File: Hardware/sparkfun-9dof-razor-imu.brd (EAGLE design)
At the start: 40.6 x 27.9 mm, 40 parts, among them J1 AVR_SPI_PRG_6PTH, Q1 8MHz, U1 ITG-32001:1, U2 ADXL3451:1, U5 3.3V, U6 ATMEGA328

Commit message: Initial commit of v24.
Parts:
- removed C13, C22, C24, C25, C27, C29: 0.1uF, SparkFun:0603-CAP
- removed C18: 0.22uF, SparkFun:0603-CAP
- removed C21: 4.7uF, SparkFun:0603-CAP
- removed C23, C26: 10uF, SparkFun:EIA3216
- removed JP10: JST_Horizontal, SparkFun:1X02
- removed JP11, JP12: FIDUCIAL1X2.5, abes:FIDUCIAL-1X2.5
- removed JP2, JP4, JP6: STAND-OFF, SparkFun:STAND-OFF
- removed JP3: LOGO-SFENEW, SparkFun:SFE-NEW-WEBLOGO
- removed JP7: FTDI Basic, SparkFun:1X06
- removed LED1: Red, SparkFun:LED-0603
- removed Q1: 8MHz, SparkFun:RESONATOR-SMD
- removed R11: 10K, SparkFun:0603-RES
- removed R12: 330, SparkFun:0603-RES
- removed S2: Power, SparkFun:AYZ0202
- removed U$1: HMC5883LSMD, SparkFun:16LPCC
- removed U$4: OSHW-LOGOL, SparkFun:OSHW-LOGO-L
- removed U5: 3.3V, SparkFun:SOT23-5
- removed U6: ATMEGA328, SparkFun:TQFP32-08
- added C10: 2.2uF, SparkFun-Capacitors:0603
- added C11, C12: 4.7uF, SparkFun-Capacitors:0603
- added C4, C5, C6: 0.1uF, SparkFun-Capacitors:0603
- added C7, C8: 15pF, SparkFun-Capacitors:0603
- added C9: 1.0uF, SparkFun-Capacitors:0603
- added D1: 1A/23V/620mV, SparkFun-DiscreteSemi:SOD-323
- added D2: RED, SparkFun-LED:LED-0603
- added D4: Yellow, SparkFun-LED:LED-0603
- added F1: 6V/0.5A, SparkFun-Fuses:1206
- added FRAME1: FRAME-LEDGER, SparkFun-Aesthetics:CREATIVE_COMMONS
- added H1, H2, H3, H4: STAND-OFF, SparkFun-Electromechanical:STAND-OFF
- added J2: (no value), SparkFun-Connectors:JST-2-SMD
- added J3: (no value), SparkFun-Connectors:1X04
- added J4: (no value), SparkFun-Connectors:USB-B-MICRO-SMD_V03
- added J5, J7: (no value), SparkFun-Connectors:1X06_NO_SILK
- added J8: (no value), SparkFun-Connectors:1X08
- added LOGO1: SFE_LOGO_FLAME.1_INCH, SparkFun-Aesthetics:SFE_LOGO_FLAME_.1
- added LOGO2: OSHW-LOGOS, SparkFun-Aesthetics:OSHW-LOGO-S
- added LOGO3: SFE_LOGO_NAME.1_INCH, SparkFun-Aesthetics:SFE_LOGO_NAME_.1
- added R3, R5: 1k, SparkFun-Resistors:0603
- added R4: 10k, SparkFun-Resistors:0603
- added R7, R8: 100k, SparkFun-Resistors:0603
- added R9: 2.2k, SparkFun-Resistors:0603
- added U3: 3.3V, SparkFun-IC-Power:SOT23-5
- added U4: MCP73831, SparkFun-IC-Power:SOT23-5
- added Y1: 32.768kHz, SparkFun-Clocks:CRYSTAL-SMD-3.2X1.5MM
- C1: device SparkFun:0603-CAP -> SparkFun-Capacitors:0603
- C2: value 2.2nF -> 0.1uF; device SparkFun:0603-CAP -> SparkFun-Capacitors:0603
- C3: value 10nF -> 0.1uF; device SparkFun:0603-CAP -> SparkFun-Capacitors:0603
- D3: value Green -> BLUE; device SparkFun:LED-0603 -> SparkFun-LED:LED-0603
- J1: value AVR_SPI_PRG_6PTH -> USD_CONNECTOR; device SparkFun:2X3 -> SparkFun-Connectors:MICRO-SD-SOCKET-PP
- JP1: value JST_Horizontal -> PWR-SELECT; device SparkFun:JST-2-SMD -> SparkFun-Jumpers:SMT-JUMPER_3_1-NC_PASTE_NO-SILK
- JP5: value STAND-OFF -> CORTEX_DEBUGPTH; device SparkFun:STAND-OFF -> samd21-temp:2X5-PTH-1.27MM
- R1: device SparkFun:0603-RES -> SparkFun-Resistors:0603
- R10: value 10K -> 1k; device SparkFun:0603-RES -> SparkFun-Resistors:0603
- R2: value 4.7K -> 4.7k; device SparkFun:0603-RES -> SparkFun-Resistors:0603
- S1: value Reset -> (none); device SparkFun:TACTILE_SWITCH_SMD -> SparkFun-Electromechanical:SWITCH-SPST-SMD-A
- U1: value ITG-32001:1 -> ATSAMD21G-A; device Testing:QFN-24_ITG3200_1:1 -> SparkFun-IC-Microcontroller:TQFP-48
- U2: value ADXL3451:1 -> MPU-9250"; device Testing:LGA14 -> 9dof-devboard-temp:QFN24-3X3
- moved JP5 30.7 mm to (7.62, 21.6), turned to 270 degrees
- moved D3 28.5 mm to (28.6, 7.62), flipped to the bottom, turned to 90 degrees
- moved C2 27.6 mm to (16.5, 28.6), turned to 180 degrees
- moved S1 24.0 mm to (2.79, 10.9), flipped to the bottom, turned to 270 degrees
- moved JP1 22.9 mm to (24.1, 29.2)
- moved C1 21.7 mm to (20.3, 25.4)
- moved R1 19.8 mm to (11.2, 26.7), turned to 90 degrees
- moved R2 18.9 mm to (12.7, 26.7), turned to 90 degrees
- moved R10 16.7 mm to (16.5, 3.68), flipped to the bottom, turned to 90 degrees
- moved U2 14.2 mm to (16.5, 25.4), turned to 90 degrees
- moved U1 10.3 mm to (15.2, 12.1), turned to 180 degrees
- moved J1 9.91 mm to (9.91, 14.2), flipped to the bottom
- moved C3 3.42 mm to (17.8, 4.45), turned to 270 degrees
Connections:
- removed net DTR: C27.2, JP7.1
- removed net MISO: J1.1, U6.16
- removed net MOSI: J1.4, U6.15
- removed net N$12: D3.A, R12.2
- removed net N$13: Q1.1, U6.8
- removed net N$14: Q1.3, U6.7
- removed net N$15: JP1.2, JP10.2, S2.2, S2.5
- removed net N$38: LED1.A, R11.1
- removed net RAW: C26.A, S2.1, S2.4, U5.1, U5.3
- removed net RESET: C27.1, J1.5, R10.1, S1.3, U6.29
- removed net RXI: JP7.3, U6.30
- removed net SCK: J1.3, R12.1, U6.17
- removed net TXO: JP7.2, U6.31
- new net !RESET: JP5.10, R4.1, U1.40
- new net A0: J8.1, U1.3
- new net A1: J8.2, U1.7
- new net A2: U1.8
- new net A3: U1.9
- new net A4: U1.10
- new net A5: U1.47
- new net CHG_LED: R10.1, U4.1
- new net D0/RXI: J8.8, U1.16
- new net D1/TXO: J8.7, U1.15
- new net D10: J8.6, U1.27
- new net D11: J8.5, U1.25
- new net D12: J8.4, U1.28
- new net D13: J8.3, R3.2, U1.26
- new net D2/SD_CD: J1.CD1, U1.23
- new net D3: U1.14
- new net D4: U1.13
- new net D5: U1.24
- new net D6: U1.29
- new net D7: U1.30
- new net D8: U1.11
- new net D9: U1.12
- new net FSYNC: U2.11
- new net INT: U2.12
- new net N$10: C11.1, D1.A, J2.2, U4.3
- new net N$11: D4.C, R10.2
- new net N$5: D2.A, R5.1
- new net N$7: R9.2, U4.5
- new net N$8: J1.RSV1, R7.1
- new net N$9: J1.RSV2, R8.1
- new net REGOUT: C1.1, U2.10
- new net RX_EDBG: U1.38
- new net RX_LED: U1.48
- new net SD_!CS!: J1.CS, U1.22
- new net SD_MISO: J1.DO, U1.21
- new net SD_MOSI: J1.DI, U1.19
- new net SD_SCK: J1.SCLK, U1.20
- new net SHIELD: J4.SHIELD1, J4.SHIELD2, J4.SHIELD3
- new net SWCLK: JP5.4, U1.45
- new net SWDIO: JP5.2, U1.46
- new net TX_EDBG: U1.37
- new net TX_LED: U1.39
- new net USB_D+: J4.D+, U1.34
- new net USB_D-: J4.D-, U1.33
- new net USB_HOST_EN: U1.41
- new net VDDCORE: C4.1, U1.43
- new net VIN: C12.1, C9.1, D1.C, D4.A, F1.2, JP1.1, S1.1, U3.1, U4.4
- new net VREG_EN: S1.2, U3.3
- net 3.3V: now also C10.1, C2.1, C5.1, C6.1, J1.VCC, J3.2, JP1.3, JP5.1, R4.2, R5.2, R7.2, R8.2, U1.17, U1.36, U1.44, U1.6, U2.13, U2.22, U2.8, U3.5; no longer C13.1, C22.1, C23.A, C24.2, C29.1, J1.2, JP7.4, R10.2, R11.2, U$1.13, U$1.2, U$1.4, U1.13, U1.8, U2.1, U2.6, U2.7, U5.5, U6.18, U6.4, U6.6
- net AREF: now also U1.4; no longer C25.2, U6.20
- net GND: now also C10.2, C11.2, C12.2, C4.2, C5.2, C6.2, C7.1, C8.2, C9.2, D2.C, J1.GND, J1.GND1, J1.GND3, J2.1, J3.1, J4.GND, J7.1, J7.2, J7.3, J7.4, J7.5, J7.6, JP5.3, JP5.5, R9.1, S1.3, U1.35, U1.42, U1.5, U2.18, U2.9, U3.2, U4.2; no longer C13.2, C21.2, C22.2, C23.C, C24.1, C25.1, C26.C, C29.2, J1.6, JP1.1, JP10.1, JP7.5, JP7.6, LED1.C, Q1.2, S1.1, U$1.11, U$1.9, U1.1, U1.11, U1.9, U2.12, U2.2, U2.4, U2.5, U5.2, U6.21, U6.3, U6.5
- net N$1: now also F1.1, J4.VBUS; no longer C18.2, U$1.8
- net N$2: now also C7.2, U1.1, Y1.P$2; no longer C18.1, U$1.12
- net N$3: now also D3.A, R3.1; no longer C1.1, U1.10
- net N$4: now also C8.1, U1.2, Y1.P$1; no longer C2.1, U1.20
- net N$6: now also J5.1, J5.2, J5.3, J5.4, J5.5, J5.6, JP1.2; no longer C21.1, U$1.10
- net SCL: now also J3.4, U1.32, U2.23; no longer U$1.1, U1.23, U2.14, U6.28
- net SDA: now also J3.3, U1.31, U2.24; no longer U$1.16, U1.24, U2.13, U6.27
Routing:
- net VIN: track 0.00 -> 61.8 mm, vias 0 -> 1
- net RESET: track 44.5 -> 0.00 mm, vias 3 -> 0
- net D13: track 0.00 -> 29.7 mm, vias 0 -> 1
- net D10: track 0.00 -> 25.1 mm, vias 0 -> 1
- net D12: track 0.00 -> 23.4 mm, vias 0 -> 1
- net !RESET: track 0.00 -> 23.3 mm
- net D11: track 0.00 -> 23.1 mm, vias 0 -> 1
- net SWDIO: track 0.00 -> 21.5 mm, vias 0 -> 1
- net D0/RXI: track 0.00 -> 20.6 mm, vias 0 -> 1
- net N$15: track 20.4 -> 0.00 mm
- net SWCLK: track 0.00 -> 20.0 mm, vias 0 -> 1
- net CHG_LED: track 0.00 -> 19.9 mm, vias 0 -> 2
- net D1/TXO: track 0.00 -> 18.0 mm, vias 0 -> 1
- net TXO: track 17.8 -> 0.00 mm, vias 1 -> 0
- net SCK: track 17.1 -> 0.00 mm, vias 2 -> 0
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- added copper zone on layer 1, net SHIELD
- added copper zone on layer 16, net SHIELD
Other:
- board size 40.6 x 27.9 mm -> 31.8 x 31.8 mm
- board text added: "0 !RX"
- board text added: "1 !TX"
- board text added: "10"
- board text added: "11"
- board text added: "12"
- board text added: "13"
- board text added: "9DoF Razor IMU"
- board text added: "A0"
- board text added: "A1"
- board text added: "ACCEL GYRO"
- board text added: "CHG"
- board text added: "MAG"
- board text added: "PWR"
- board text added: "SCL"
- board text added: "SDA"
- board text added: "VBUS"
- board text added: "VIN"
- board text added: "v24"
- board text removed: "+"
- board text removed: "-"
- board text removed: "9DOF RAZOR"
- board text removed: "BLK"
- board text removed: "CTS"
- board text removed: "DTR"
- board text removed: "GRN"
- board text removed: "RXI"
- board text removed: "Reset"
- board text removed: "Stat"
- board text removed: "TXO"
- board text removed: "v23"

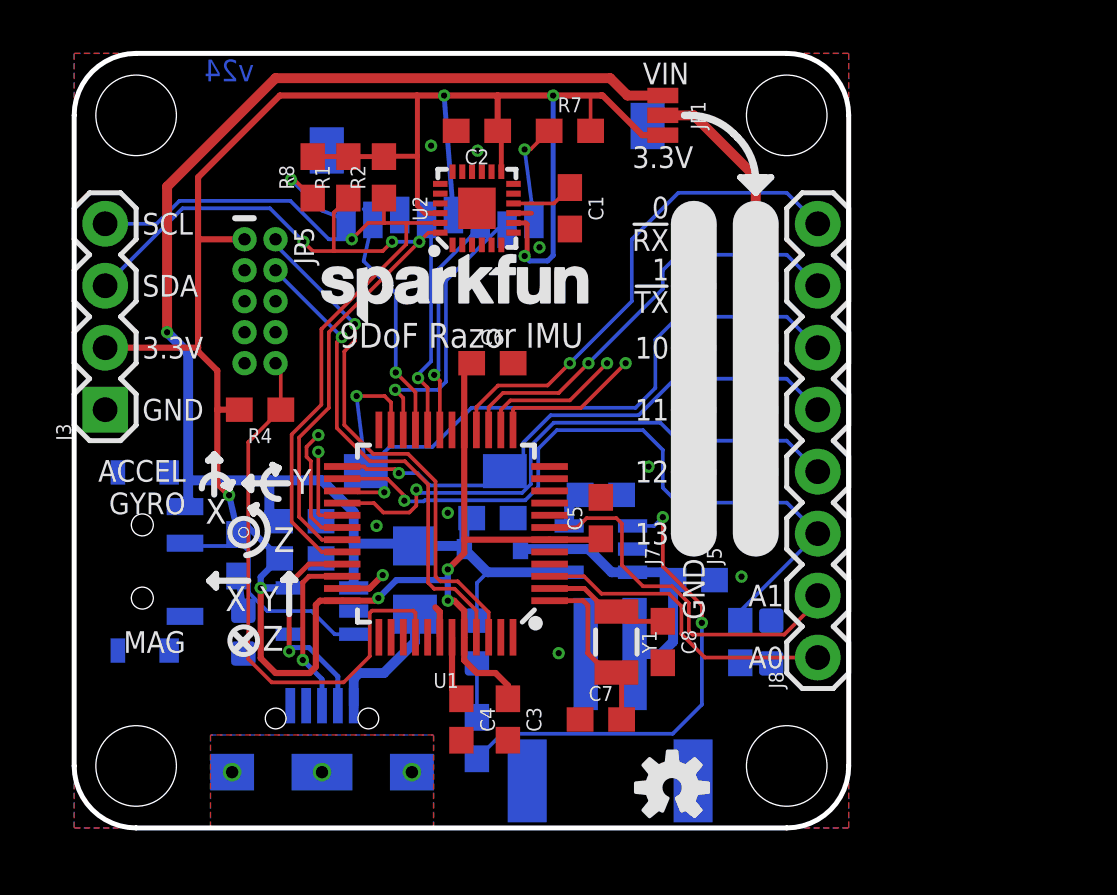
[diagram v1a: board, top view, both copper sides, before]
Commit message: Schematic cleanup, bottom re-routing.
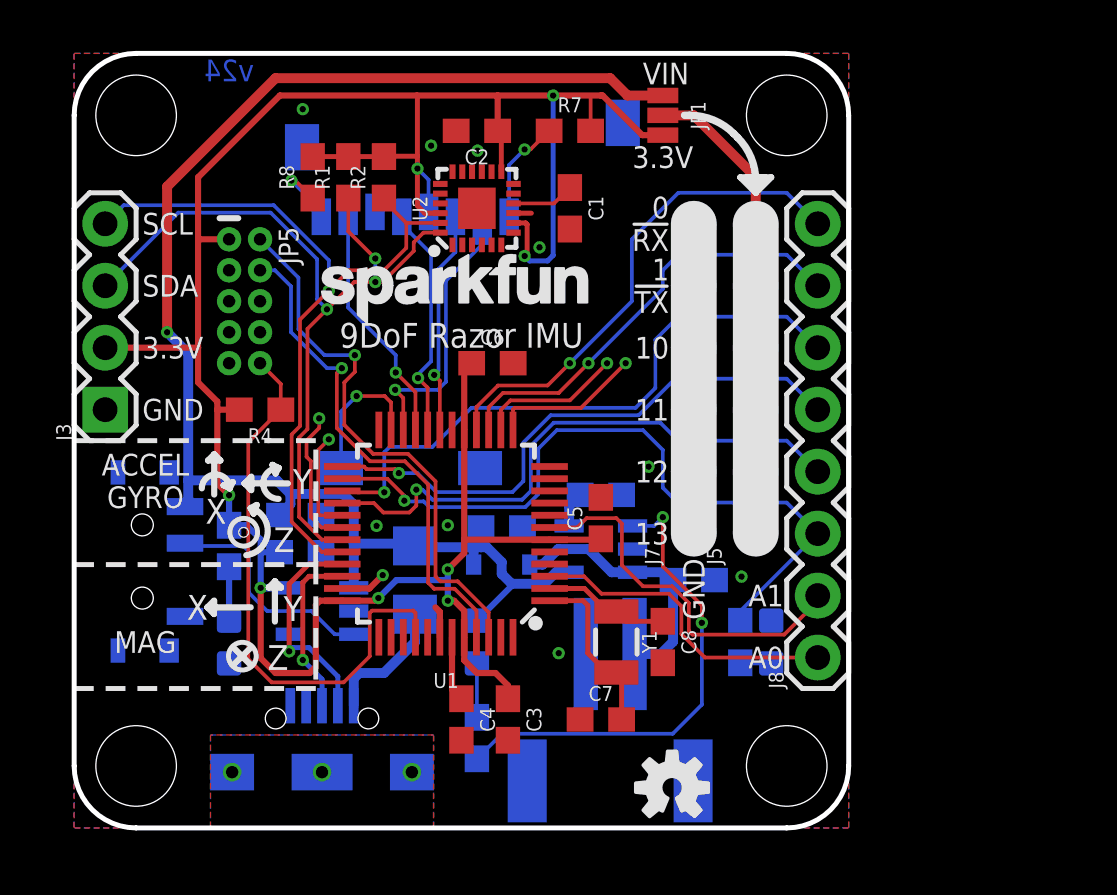
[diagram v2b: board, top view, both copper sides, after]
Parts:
- FRAME1: value FRAME-LEDGER -> FRAME-LETTER
- JP1: value PWR-SELECT -> PW-RAIL
- moved FRAME1 10.2 mm to (20.3, -11.4)
- moved J1 1.02 mm to (8.89, 14.4)
- moved D1 0.74 mm to (17.5, 10.8)
- moved D2 0.71 mm to (6.35, 7.62)
- moved JP5 0.63 mm to (6.99, 21.6)
- moved R5 0.54 mm to (6.35, 11.6)
- moved C12 0.54 mm to (17.5, 12.3)
- moved C10 0.25 mm to (9.27, 11.3)
- moved C9 0.25 mm to (9.27, 12.8)
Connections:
- net USB_D+ renamed D+
- net USB_D- renamed D-
- removed net AREF: U1.4
- removed net RX_EDBG: U1.38
- removed net TX_EDBG: U1.37
- removed net TX_LED: U1.39
- removed net USB_HOST_EN: U1.41
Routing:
- net 3.3V: track 113.3 -> 109.6 mm
- net SWDIO: track 21.5 -> 22.5 mm
- net SWCLK: track 20.0 -> 20.9 mm
- net N$9: track 4.05 -> 3.17 mm
- net SCL: track 32.9 -> 32.1 mm
- net N$5: track 1.44 -> 2.21 mm
- net D7: track 5.09 -> 5.80 mm
- net D6: track 3.55 -> 4.24 mm
- net SD_!CS!: track 11.5 -> 11.0 mm
- net GND: vias 9 -> 10

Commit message: Cleaning up routing.
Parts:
- moved D3 1.27 mm to (27.3, 7.62)
- moved R3 1.27 mm to (28.6, 7.62)
- moved D4 0.64 mm to (15.9, 7.62)
- moved R10 0.64 mm to (15.9, 3.68)
- moved Y1 0.25 mm to (22.0, 7.62)
- moved U4 0.25 mm to (21.6, 11.2)
- moved R9 0.13 mm to (21.6, 13.5), turned to 180 degrees
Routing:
- net D13: track 30.1 -> 26.6 mm
- net D12: track 23.8 -> 22.3 mm
- net N$7: track 1.46 -> 2.73 mm
- net D11: track 23.3 -> 22.4 mm
- net CHG_LED: track 19.9 -> 20.6 mm
- net VIN: track 61.9 -> 62.6 mm
- net GND: track 3.92 -> 3.90 mm, vias 10 -> 11

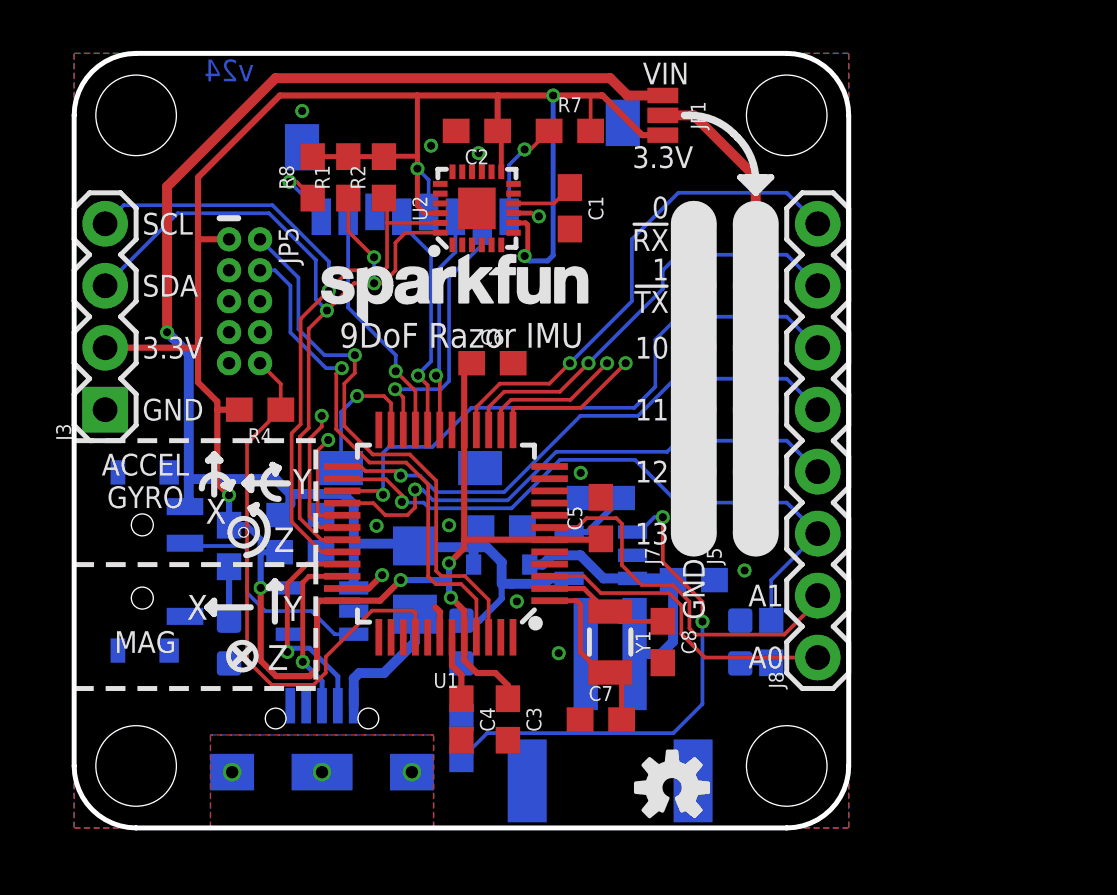
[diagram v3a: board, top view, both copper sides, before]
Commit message: Brd/sch tweaks after engineer checklist.
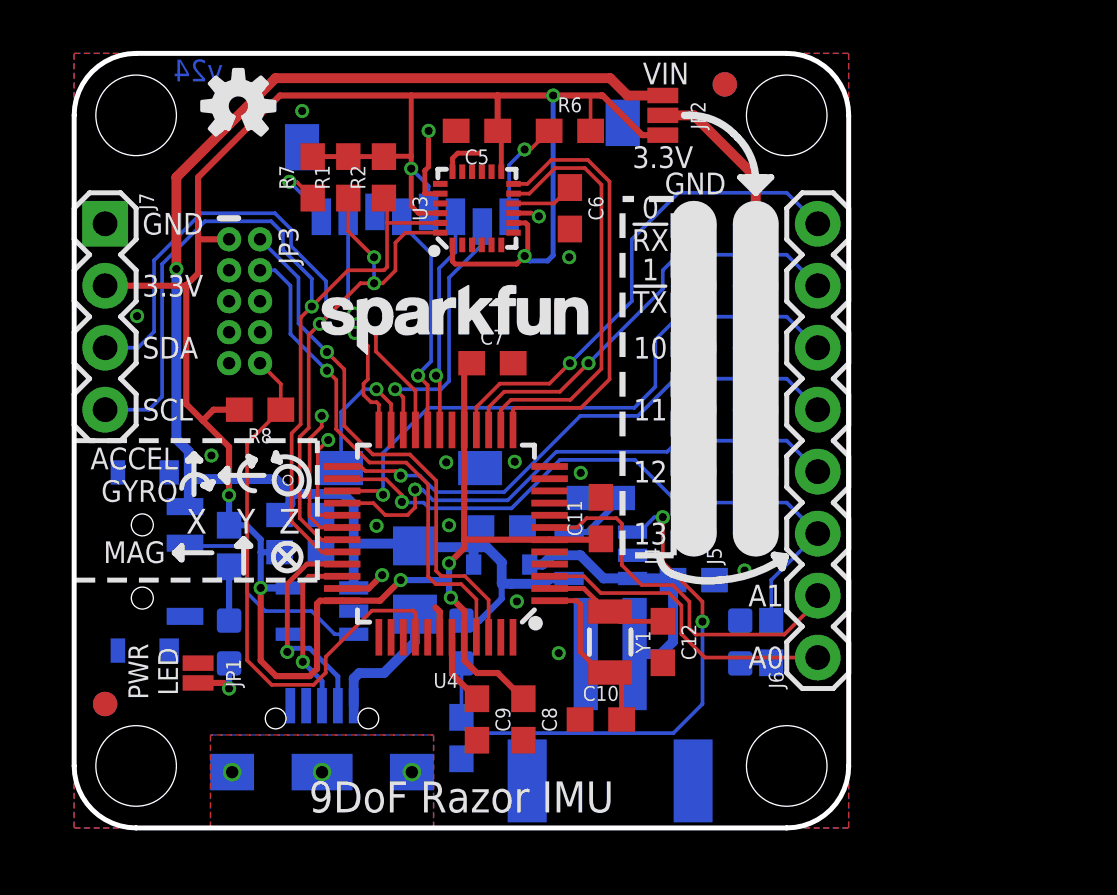
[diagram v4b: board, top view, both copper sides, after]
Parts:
- removed R10: 1k, SparkFun-Resistors:0603
- added FD1, FD2, FD3, FD4: FIDUCIAL1X2, SparkFun-Aesthetics:FIDUCIAL-1X2
- added JP2: PWR, SparkFun-Jumpers:SMT-JUMPER_3_1-NC_PASTE_NO-SILK
- added R6: 100k, SparkFun-Resistors:0603
- C1: value 0.1uF -> 1.0uF
- C10: value 2.2uF -> 15pF
- C11: value 4.7uF -> 0.1uF
- C12: value 4.7uF -> 15pF
- C2: value 0.1uF -> 2.2uF
- C3, C4: value 0.1uF -> 4.7uF
- C7, C8: value 15pF -> 0.1uF
- C9: value 1.0uF -> 0.1uF
- D2: value RED -> Yellow
- D3: value BLUE -> RED
- D4: value Yellow -> BLUE
- J1: value USD_CONNECTOR -> LiPo; device SparkFun-Connectors:MICRO-SD-SOCKET-PP -> SparkFun-Connectors:JST-2-SMD
- J2: device SparkFun-Connectors:JST-2-SMD -> SparkFun-Connectors:USB-B-MICRO-SMD_V03
- J3: value (none) -> USD_CONNECTOR; device SparkFun-Connectors:1X04 -> SparkFun-Connectors:MICRO-SD-SOCKET-PP
- J4: device SparkFun-Connectors:USB-B-MICRO-SMD_V03 -> SparkFun-Connectors:1X06_NO_SILK
- J7: device SparkFun-Connectors:1X06_NO_SILK -> SparkFun-Connectors:1X04
- JP1: value PW-RAIL -> LED; device SparkFun-Jumpers:SMT-JUMPER_3_1-NC_PASTE_NO-SILK -> SparkFun-Jumpers:SMT-JUMPER_2_NC_PASTE_NO-SILK
- R4: value 10k -> 2.2k
- R8: value 100k -> 10k
- R9: value 2.2k -> 1k
- U1: value ATSAMD21G-A -> 3.3V; device SparkFun-IC-Microcontroller:TQFP-48 -> SparkFun-IC-Power:SOT23-5
- U2: value MPU-9250" -> MCP73831; device 9dof-devboard-temp:QFN24-3X3 -> SparkFun-IC-Power:SOT23-5
- U3: value 3.3V -> MPU-9250"; device SparkFun-IC-Power:SOT23-5 -> 9dof-devboard-temp:QFN24-3X3
- U4: value MCP73831 -> ATSAMD21G-A; device SparkFun-IC-Power:SOT23-5 -> SparkFun-IC-Microcontroller:TQFP-48
- moved FRAME1 37.4 mm to (-16.5, -17.8)
- moved LOGO2 33.1 mm to (6.73, 29.6)
- moved JP1 29.8 mm to (5.08, 6.35)
- moved J7 27.3 mm to (1.27, 24.8), turned to 270 degrees
- moved H3 26.7 mm to (29.2, 29.2)
- moved H4 26.7 mm to (2.54, 29.2)
- moved R3 22.6 mm to (6.35, 11.6)
- moved D3 21.0 mm to (6.35, 7.62), turned to 270 degrees
- moved C2 18.7 mm to (9.27, 11.3), flipped to the bottom
- moved J4 18.1 mm to (25.4, 12.1), flipped to the top
- moved U3 17.7 mm to (16.5, 25.4), flipped to the top, turned to 90 degrees
- moved J1 17.0 mm to (22.0, 3.43), turned to 180 degrees
- moved C1 16.7 mm to (9.27, 12.8), flipped to the bottom, turned to 180 degrees
- moved C5 16.7 mm to (16.5, 28.6), turned to 180 degrees
- moved C7 15.3 mm to (17.1, 19.1)
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- renumbered J8 to J6, JP5 to JP3
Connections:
- removed net A2: U1.8
- removed net A3: U1.9
- removed net A4: U1.10
- removed net A5: U1.47
- removed net D3: U1.14
- removed net D4: U1.13
- removed net D8: U1.11
- removed net D9: U1.12
- removed net FSYNC: U2.11
- removed net INT: U2.12
- removed net N$5 (its old number): D2.A, R5.1
- removed net RX_LED: U1.48
- new net D3/FSYNC: U3.11, U4.14
- new net D4/INT: U3.12, U4.13
- new net N$12: D3.C, JP1.2
- new net N$3: D4.A, R9.1
- net !RESET: now also R8.1, U4.40; no longer R4.1, U1.40
- net 3.3V: now also C11.1, C7.1, C8.1, J3.VCC, J7.2, JP2.3, R3.2, R6.2, U1.5, U3.1, U3.13, U3.22, U3.8, U4.17, U4.36, U4.44, U4.6; no longer C10.1, C3.1, C6.1, J1.VCC, J3.2, JP1.3, R4.2, R5.2, U1.17, U1.36, U1.44, U1.6, U2.13, U2.22, U2.8, U3.5
- net A0: now also U4.3; no longer U1.3
- net A1: now also U4.7; no longer U1.7
- net CHG_LED: now also R5.1, U2.1; no longer R10.1, U4.1
- net D+: now also J2.D+, U4.34; no longer J4.D+, U1.34
- net D-: now also J2.D-, U4.33; no longer J4.D-, U1.33
- net D0/RXI: now also U4.16; no longer U1.16
- net D1/TXO: now also U4.15; no longer U1.15
- net D10: now also U4.27; no longer U1.27
- net D11: now also U4.25; no longer U1.25
- net D12: now also U4.28; no longer U1.28
- net D13: now also R9.2, U4.26; no longer R3.2, U1.26
- net D2/SD_CD: now also J3.CD1, U4.23; no longer J1.CD1, U1.23
- net D5: now also U4.24; no longer U1.24
- net D6: now also U4.29; no longer U1.29
- net D7: now also U4.30; no longer U1.30
- net GND: now also C10.1, C7.2, D4.C, J1.1, J2.GND, J3.GND, J3.GND1, J3.GND3, J4.1, J4.2, J4.3, J4.4, J4.5, J4.6, JP1.1, R4.1, U1.2, U2.2, U3.18, U3.20, U3.9, U4.18, U4.35, U4.42, U4.5; no longer C10.2, C7.1, D2.C, D3.C, J1.GND, J1.GND1, J1.GND3, J2.1, J3.1, J4.GND, J7.2, J7.3, J7.4, J7.5, J7.6, R9.1, U1.18, U1.35, U1.42, U1.5, U2.18, U2.9, U3.2, U4.2
- net N$1: now also J2.VBUS; no longer J4.VBUS
- net N$10: now also C4.1, J1.2, U2.3; no longer C11.1, J2.2, U4.3
- net N$11: now also D2.C, R5.2; no longer D4.C, R10.2
- net N$2: now also C10.2, U4.1; no longer C7.2, U1.1
- net N$4: now also C12.1, U4.2; no longer C8.1, U1.2
- net N$6: now also JP2.2; no longer JP1.2
- net N$7: now also R4.2, U2.5; no longer R9.2, U4.5
- net N$8: now also J3.RSV1, R6.1; no longer J1.RSV1, R7.1
- net N$9: now also J3.RSV2, R7.1; no longer J1.RSV2, R8.1
- net REGOUT: now also C6.1, U3.10; no longer C1.1, U2.10
- net SCL: now also J7.4, U3.23, U4.32; no longer J3.4, U1.32, U2.23
- net SDA: now also J7.3, U3.24, U4.31; no longer J3.3, U1.31, U2.24
- net SD_!CS!: now also J3.CS, U4.22; no longer J1.CS, U1.22
- net SD_MISO: now also J3.DO, U4.21; no longer J1.DO, U1.21
- net SD_MOSI: now also J3.DI, U4.19; no longer J1.DI, U1.19
- net SD_SCK: now also J3.SCLK, U4.20; no longer J1.SCLK, U1.20
- net SHIELD: now also J2.SHIELD1, J2.SHIELD2, J2.SHIELD3; no longer J4.SHIELD1, J4.SHIELD2, J4.SHIELD3
- net SWCLK: now also U4.45; no longer U1.45
- net SWDIO: now also U4.46; no longer U1.46
- net VDDCORE: now also C9.1, U4.43; no longer C4.1, U1.43
- net VIN: now also C1.1, C3.1, D2.A, JP2.1, U1.1, U2.4; no longer C12.1, C9.1, D4.A, JP1.1, U3.1, U4.4
- net VREG_EN: now also U1.3; no longer U3.3
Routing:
- net D4/INT: track 0.00 -> 18.1 mm
- net D3/FSYNC: track 0.00 -> 17.5 mm
- net D4: track 6.24 -> 0.00 mm, vias 1 -> 0
- net D3: track 5.97 -> 0.00 mm, vias 1 -> 0
- net SCL: track 32.2 -> 37.9 mm
- net GND: track 3.90 -> 8.87 mm, vias 11 -> 15
- net 3.3V: track 109.7 -> 114.6 mm
- net D5: track 0.00 -> 4.67 mm, vias 0 -> 1
- net SDA: track 34.6 -> 38.0 mm
- net N$12: track 0.00 -> 2.39 mm, vias 0 -> 1
- net N$5 (its old number): track 2.21 -> 0.00 mm
- net N$3: track 0.00 -> 1.28 mm
- net SWDIO: track 22.7 -> 21.6 mm
- net N$5: track 1.28 -> 2.21 mm
- net SWCLK: track 21.1 -> 20.6 mm
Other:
- board text added: "+"
- board text added: "-"
- board text added: "Jim Lindblom"
- board text added: "PWR LED"
- board text added: "Units in inches"
